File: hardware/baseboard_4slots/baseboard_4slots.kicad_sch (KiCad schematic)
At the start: 61 parts, among them J1 IO-Board_00, J10 Conn_01x04_Male, J11 Conn_01x04_Male, J12 Conn_01x04_Male, J13 Conn_01x04_Male, J14 Conn_01x04_Male, J15 Conn_02x02_Odd_Even, J2 IO-Board_01, J3 IO-Board_10, J4 IO-Board_11, J5 USB_B_Micro, J6 Conn_01x05: Adafruit 1833, J7 Screw_Terminal_01x04, J8 Conn_02x02_Odd_Even, J9 Conn_02x02_Odd_Even, U1 NRF24L01_Breakout, U2 Pico, U3 W5500_Mini

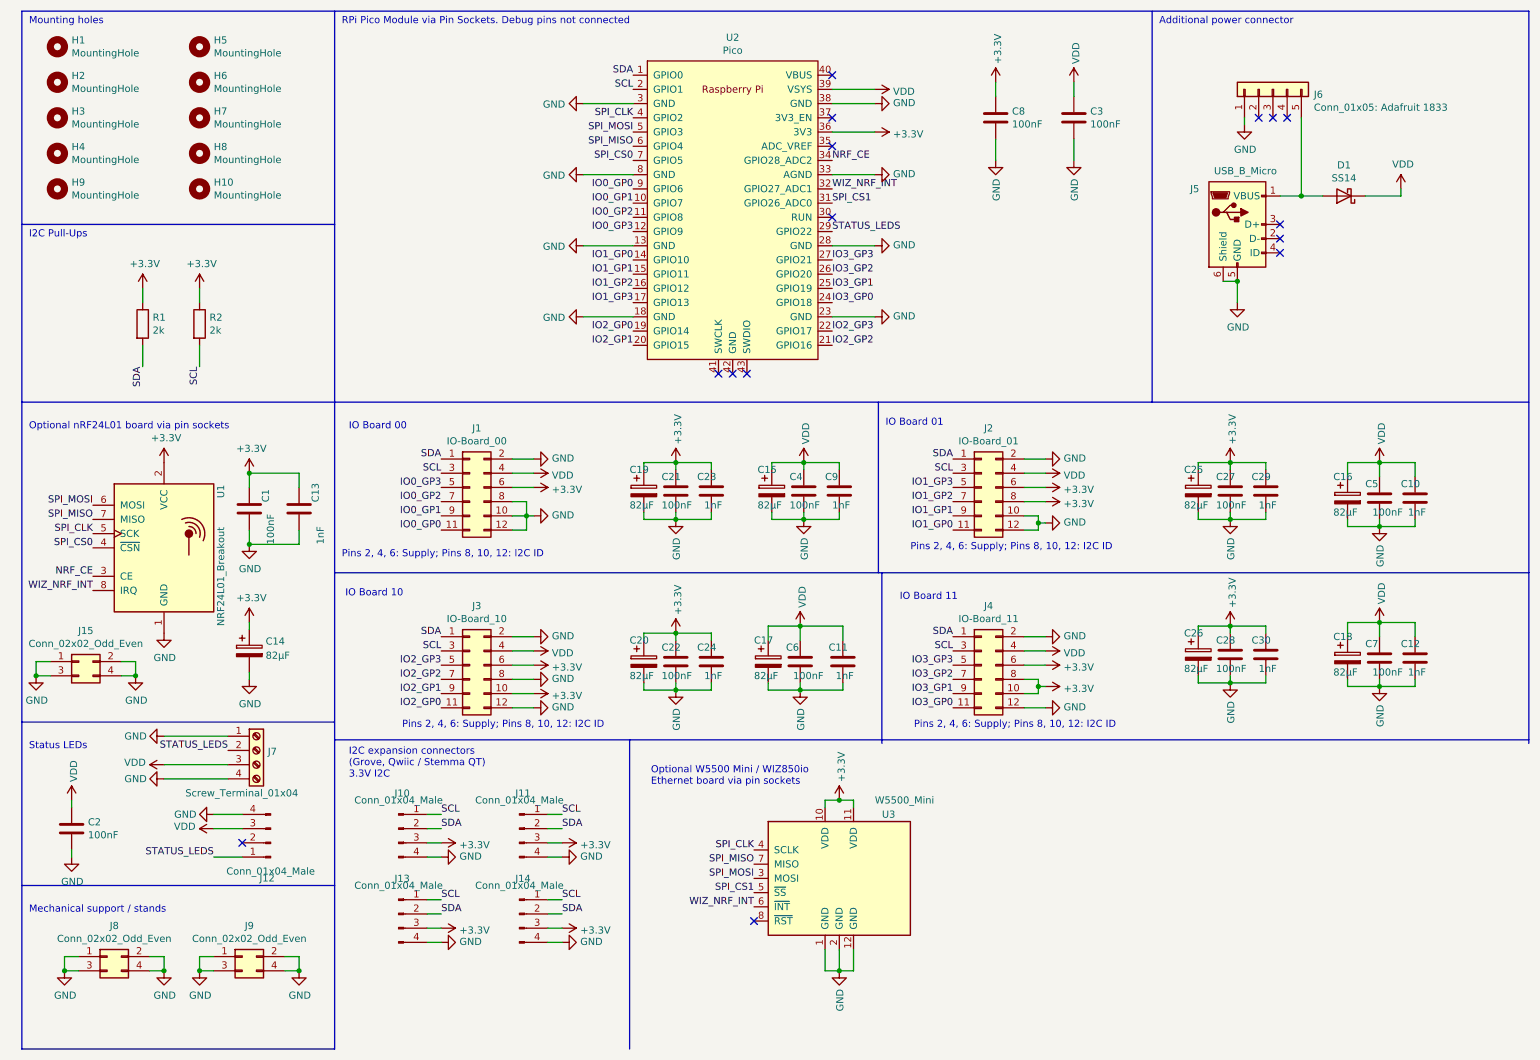
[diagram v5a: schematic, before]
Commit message: Hardware: Baseboard 4 slots: Don't let W5500 and nRF24 share the IRQ line, add a solder jumper instead
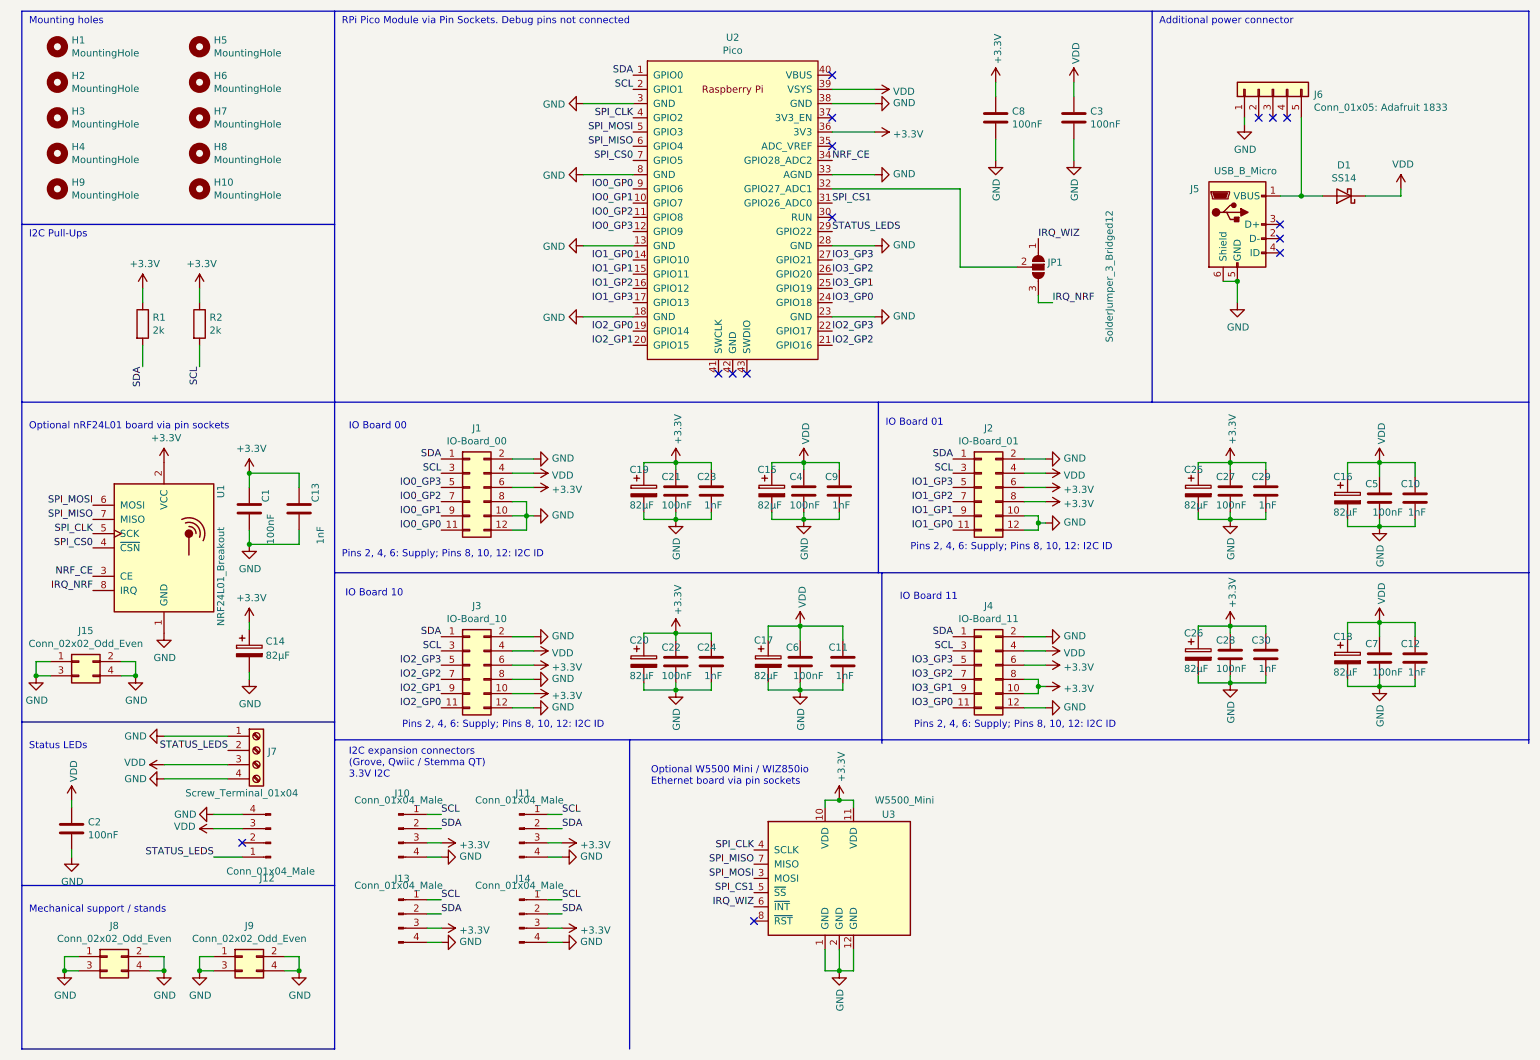
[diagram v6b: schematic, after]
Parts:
- added JP1: SolderJumper_3_Bridged12, Jumper:SolderJumper-3_P2.0mm_Open_TrianglePad1.0x1.5mm_NumberLabels, symbol Jumper:SolderJumper_3_Open
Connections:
- removed net WIZ_NRF_INT: U1.8 (IRQ), U2.32 (GPIO27_ADC1), U3.6 (~{INT})
- new net: JP1.2 (C), U2.32 (GPIO27_ADC1)
- new net IRQ_NRF: JP1.3 (B), U1.8 (IRQ)
- new net IRQ_WIZ: JP1.1 (A), U3.6 (~{INT})
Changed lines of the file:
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@@
   (title_block
     (title "rp2040_dongle baseboard 4 slots")
-    (date "2022-11-30")
-    (rev "0.6")
+    (date "2023-01-23")
+    (rev "0.7")
     (company "https://www.openlighting.org/")
   )
@@
     (stroke (width 0) (type default) (color 0 0 0 0))
   )
+  (wire (pts (xy 157.48 44.45) (xy 180.34 44.45))
+    (stroke (width 0) (type default) (color 0 0 0 0))
+  )
   (wire (pts (xy 255.27 124.46) (xy 255.27 121.92))
     (stroke (width 0) (type default) (color 0 0 0 0))
@@
     (stroke (width 0) (type default) (color 0 0 0 0))
   )
+  (wire (pts (xy 194.31 64.77) (xy 196.85 64.77))
+    (stroke (width 0) (type default) (color 0 0 0 0))
+  )
   (wire (pts (xy 241.3 31.75) (xy 241.3 45.72))
     (stroke (width 0) (type default) (color 0 0 0 0))
@@
     (stroke (width 0) (type default) (color 0 0 0 0))
   )
+  (wire (pts (xy 194.31 63.5) (xy 194.31 64.77))
+    (stroke (width 0) (type default) (color 0 0 0 0))
+  )
   (wire (pts (xy 229.87 60.96) (xy 227.33 60.96))
     (stroke (width 0) (type default) (color 0 0 0 0))
@@
     (stroke (width 0) (type default) (color 0 0 0 0))
   )
+  (wire (pts (xy 180.34 44.45) (xy 180.34 58.42))
+    (stroke (width 0) (type default) (color 0 0 0 0))
+  )
   (wire (pts (xy 228.6 122.555) (xy 234.95 122.555))
     (stroke (width 0) (type default) (color 0 0 0 0))
@@
     (stroke (width 0) (type default) (color 0 0 0 0))
   )
+  (wire (pts (xy 180.34 58.42) (xy 190.5 58.42))
+    (stroke (width 0) (type default) (color 0 0 0 0))
+  )
   (wire (pts (xy 255.27 93.345) (xy 255.27 95.885))
     (stroke (width 0) (type default) (color 0 0 0 0))
@@
     (effects (font (size 1.27 1.27)) (justify right bottom))
   )
-  (label "WIZ_NRF_INT" (at 157.48 44.45 0)
-    (effects (font (size 1.27 1.27)) (justify left bottom))
-  )
   (label "SCL" (at 179.07 127 180)
     (effects (font (size 1.27 1.27)) (justify right bottom))
@@
     (effects (font (size 1.27 1.27)) (justify right bottom))
   )
-  (label "WIZ_NRF_INT" (at 143.51 172.72 180)
+  (label "IRQ_WIZ" (at 143.51 172.72 180)
     (effects (font (size 1.27 1.27)) (justify right bottom))
   )
@@
     (effects (font (size 1.27 1.27)) (justify right bottom))
   )
+  (label "IRQ_NRF" (at 196.85 64.77 0)
+    (effects (font (size 1.27 1.27)) (justify left bottom))
+  )
   (label "STATUS_LEDS" (at 157.48 52.07 0)
     (effects (font (size 1.27 1.27)) (justify left bottom))
@@
     (effects (font (size 1.27 1.27)) (justify right bottom))
   )
-  (label "WIZ_NRF_INT" (at 25.4 116.205 180)
+  (label "IRQ_NRF" (at 25.4 116.205 180)
     (effects (font (size 1.27 1.27)) (justify right bottom))
   )
@@
     (effects (font (size 1.27 1.27)) (justify right bottom))
   )
+  (label "IRQ_WIZ" (at 194.31 53.34 0)
+    (effects (font (size 1.27 1.27)) (justify left bottom))
+  )
   (label "IO0_GP0" (at 121.92 44.45 180)
     (effects (font (size 1.27 1.27)) (justify right bottom))
@@
     (pin "1")
   )
+  (symbol (lib_id "Jumper:SolderJumper_3_Open") (at 194.31 58.42 270) (unit 1)
+    (in_bom yes) (on_board yes)
+    (property "Reference" "JP1" (id 0) (at 195.961 57.5853 90)
+      (effects (font (size 1.27 1.27)) (justify left))
+    )
+    (property "Value" "SolderJumper_3_Bridged12" (id 1) (at 207.01 48.26 0)
+      (effects (font (size 1.27 1.27)) (justify left))
+    )
+    (property "Footprint" "Jumper:SolderJumper-3_P2.0mm_Open_TrianglePad1.0x1.5mm_NumberLabels" (id 2) (at 194.31 58.42 0)
+      (effects (font (size 1.27 1.27)) hide)
+    )
+    (property "Datasheet" "~" (id 3) (at 194.31 58.42 0)
+      (effects (font (size 1.27 1.27)) hide)
+    )
+    (pin "1")
+    (pin "2")
+    (pin "3")
+  )
   (symbol (lib_id "Device:C_Polarized") (at 146.685 98.425 0) (unit 1)
     (in_bom yes) (on_board yes)
@@
       (reference "J15") (unit 1) (value "Conn_02x02_Odd_Even") (footprint "Connector_PinSocket_2.54mm:PinSocket_2x02_P2.54mm_Vertical")
     )
+    (path "/dfef8540-e81e-4032-86d6-42cda057b3ae"
+      (reference "JP1") (unit 1) (value "SolderJumper_3_Bridged12") (footprint "Jumper:SolderJumper-3_P2.0mm_Open_TrianglePad1.0x1.5mm_NumberLabels")
+    )
     (path "/00000000-0000-0000-0000-00006053cea4"

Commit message: Update baseboards to KiCad 8, add copper keepout underneath Picos, add OpenHardware logo
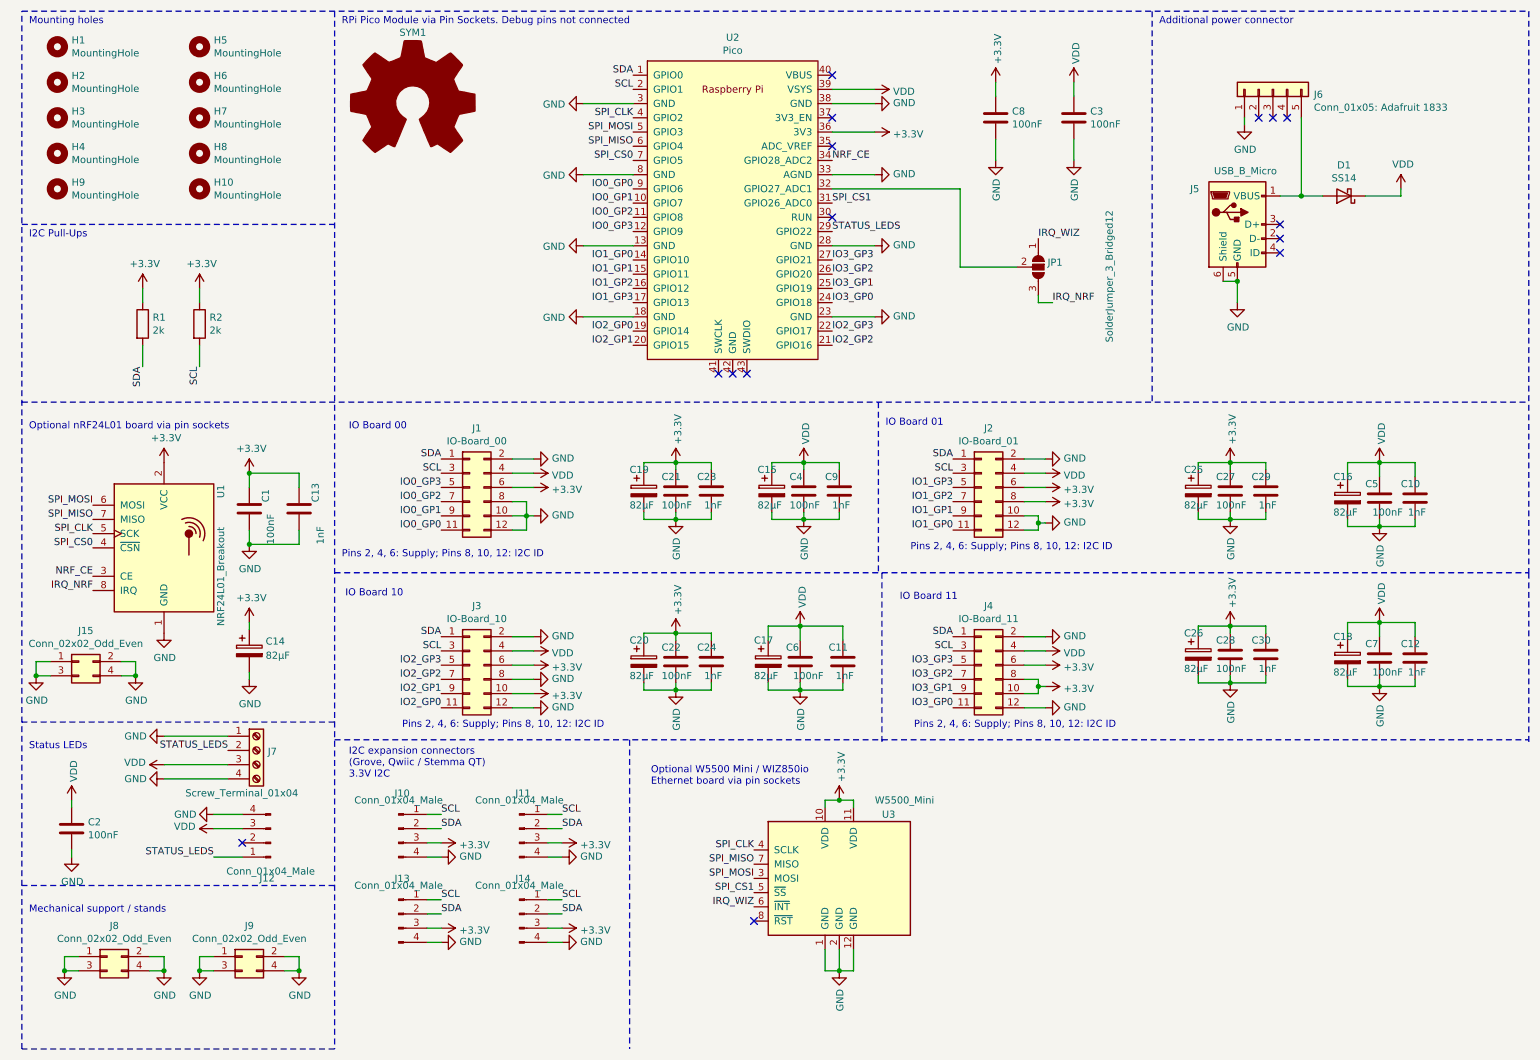
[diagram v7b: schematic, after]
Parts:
- added SYM1: Logo_Open_Hardware_Large, Symbol:OSHW-Logo2_14.6x12mm_SilkScreen, symbol Graphic:Logo_Open_Hardware_Large
